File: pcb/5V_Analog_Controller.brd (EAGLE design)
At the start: 50 x 36 mm, 26 parts, among them J1 POWER, Q1 AO3400, Q2 AO3400, U1 ESP32-PICO-MINI-02, U2 AP2112K, X1 PROG, X2 SS-52100-001, X3 SS-52100-001, X5 BOOT, X6 RESET

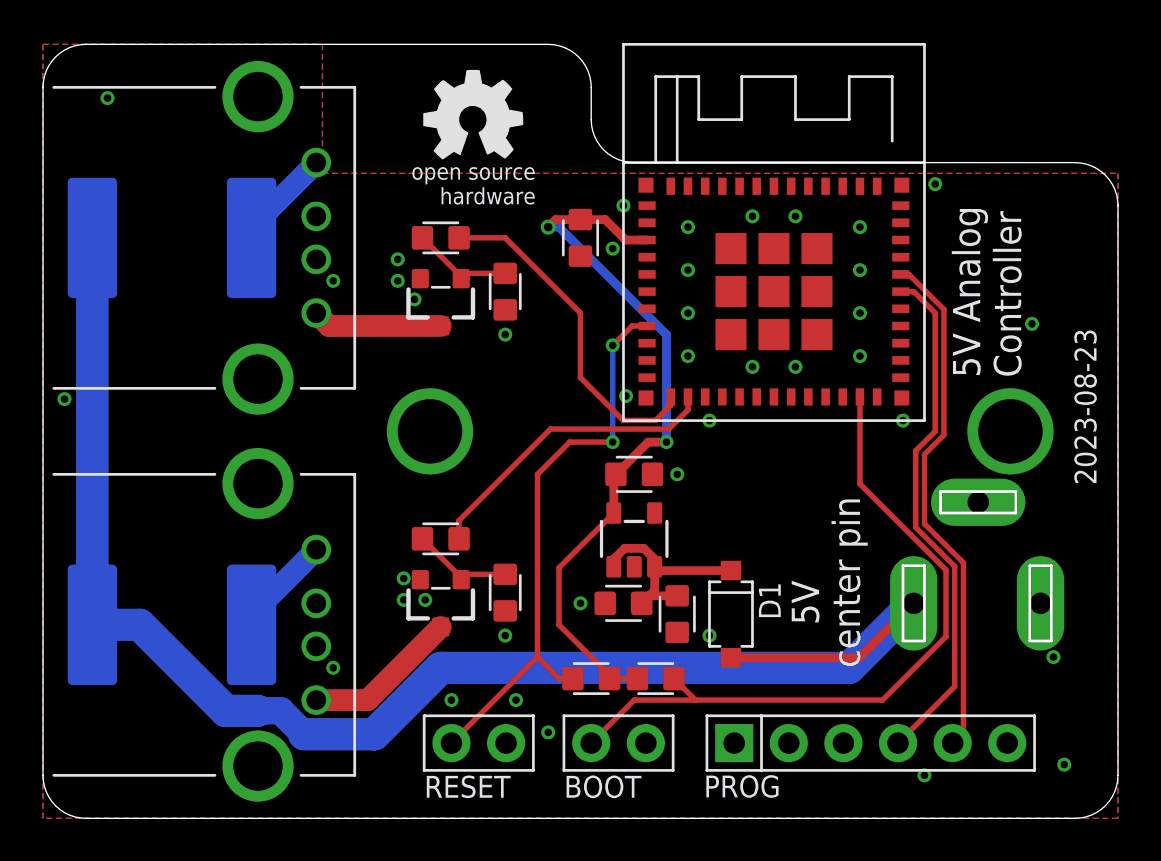
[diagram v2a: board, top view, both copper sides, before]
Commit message: Add second PTC footprint
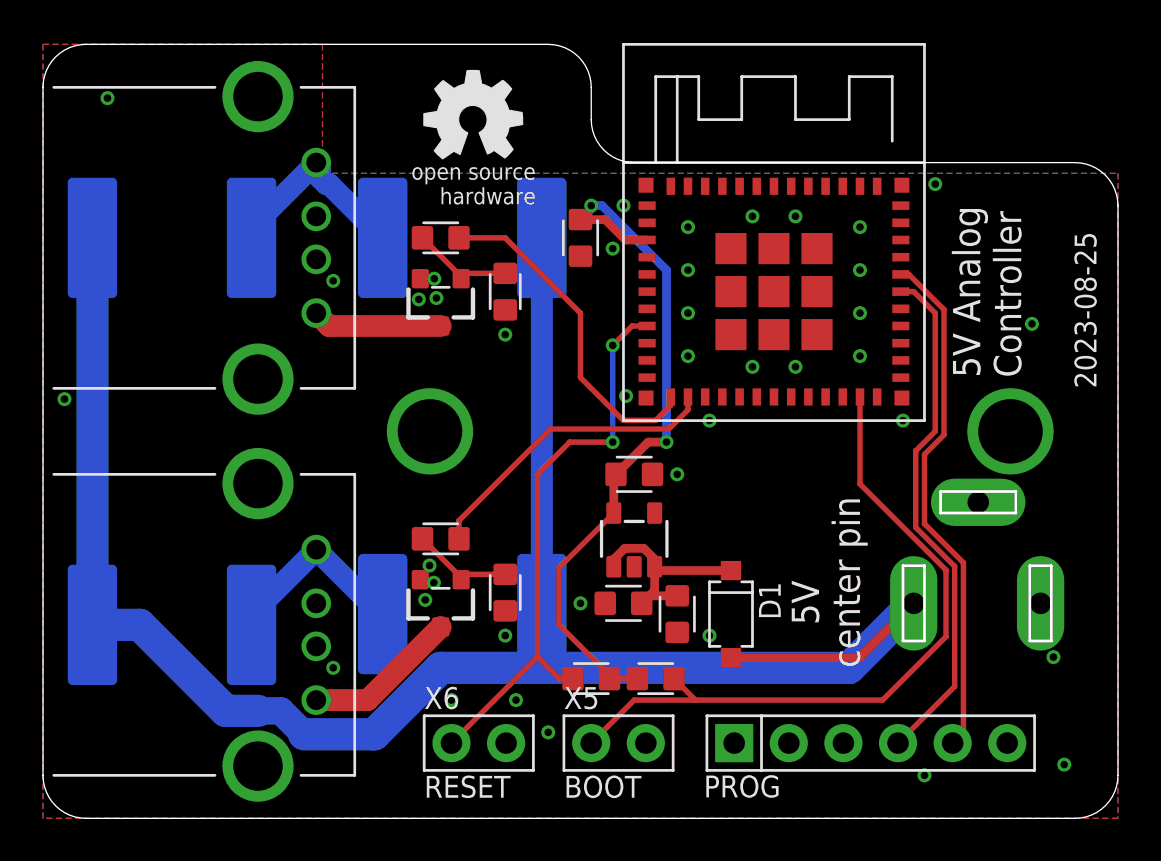
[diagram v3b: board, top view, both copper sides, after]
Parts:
- added F3, F4: JK-SMD300L-16, M2M-Fuse:JK-SMD300
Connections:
- net N$5: now also F3.B
- net N$6: now also F4.B
- net VSW: now also F3.A, F4.A
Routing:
- net VSW: track 70.4 -> 90.7 mm
- net N$5: track 4.75 -> 9.60 mm
- net N$6: track 4.75 -> 9.08 mm
- net VCC: track 33.6 -> 33.0 mm
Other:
- board text added: "2023-08-25"
- board text removed: "2023-08-23"
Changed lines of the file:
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@@
 <text x="45.5" y="20.5" size="1.27" layer="21" rot="R90">5V Analog
 Controller</text>
-<text x="49" y="15.5" size="1.016" layer="21" rot="R90">2023-08-23</text>
+<text x="49" y="20" size="1.016" layer="21" rot="R90">2023-08-25</text>
 <text x="38" y="7" size="1.27" layer="21" rot="R90">    5V
 center pin</text>
@@
 </element>
 <element name="X5" library="M2M-Connectors" package="1X02-2.54" value="BOOT" x="25.5" y="3.5" smashed="yes">
-<attribute name="NAME" x="24.23" y="5.0875" size="1.016" layer="25"/>
 <attribute name="NAME" x="24.611" y="2.865" size="1.27" layer="48"/>
 <attribute name="NAME" x="24.865" y="2.865" size="0.8128" layer="51"/>
+<attribute name="NAME" x="24.23" y="5.0875" size="1.016" layer="25"/>
 <attribute name="VALUE" x="24.23" y="0.96" size="1.016" layer="21"/>
 </element>
 <element name="X6" library="M2M-Connectors" package="1X02-2.54" value="RESET" x="19" y="3.5" smashed="yes">
-<attribute name="NAME" x="17.73" y="5.0875" size="1.016" layer="25"/>
 <attribute name="NAME" x="18.111" y="2.865" size="1.27" layer="48"/>
 <attribute name="NAME" x="18.865" y="2.365" size="0.8128" layer="51"/>
+<attribute name="NAME" x="17.73" y="5.0875" size="1.016" layer="25"/>
 <attribute name="VALUE" x="17.73" y="0.96" size="1.016" layer="21"/>
 </element>
@@
 <attribute name="NAME" x="33.3" y="11" size="1.016" layer="21" rot="R270"/>
 <attribute name="VALUE" x="29.7" y="11" size="1.016" layer="27" rot="R270"/>
+</element>
+<element name="F3" library="M2M-Fuse" package="JK-SMD300" value="JK-SMD300L-16" x="19.5" y="27" smashed="yes" rot="MR0">
+<attribute name="NAME" x="24.5" y="30.5" size="1.016" layer="26" rot="MR0"/>
+<attribute name="NAME" x="19.5" y="27" size="1.016" layer="48" rot="MR0" align="center"/>
+<attribute name="VALUE" x="24.5" y="22.5" size="1.016" layer="28" rot="MR0"/>
+</element>
+<element name="F4" library="M2M-Fuse" package="JK-SMD300" value="JK-SMD300L-16" x="19.5" y="9.5" smashed="yes" rot="MR0">
+<attribute name="NAME" x="24.5" y="13" size="1.016" layer="26" rot="MR0"/>
+<attribute name="NAME" x="19.5" y="9.5" size="1.016" layer="48" rot="MR0" align="center"/>
+<attribute name="VALUE" x="24.5" y="5" size="1.016" layer="28" rot="MR0"/>
 </element>
 </elements>
@@
 <wire x1="26.15" y1="27.85" x2="25" y2="27.85" width="0.4064" layer="1"/>
 <wire x1="27.1" y1="26.9" x2="26.15" y2="27.85" width="0.4064" layer="1"/>
-<wire x1="25" y1="27.85" x2="23.85" y2="27.85" width="0.4064" layer="1"/>
-<wire x1="23.85" y1="27.85" x2="23.5" y2="27.5" width="0.4064" layer="1"/>
-<via x="23.5" y="27.5" extent="1-16" drill="0.4"/>
 <contactref element="U2" pad="5"/>
 <contactref element="C4" pad="1"/>
@@
 <wire x1="28.15" y1="17.5" x2="29" y2="17.5" width="0.4064" layer="1"/>
 <via x="29" y="17.5" extent="1-16" drill="0.35"/>
-<wire x1="29" y1="17.5" x2="29" y2="22.5" width="0.4064" layer="16"/>
-<wire x1="29" y1="22.5" x2="24" y2="27.5" width="0.4064" layer="16"/>
-<wire x1="24" y1="27.5" x2="23.5" y2="27.5" width="0.4064" layer="16"/>
 <contactref element="R5" pad="2"/>
 <contactref element="R6" pad="2"/>
@@
 <wire x1="26.5" y1="6.5" x2="27.65" y2="6.5" width="0.254" layer="1"/>
 <wire x1="26.55" y1="14.2" x2="24" y2="11.65" width="0.254" layer="1"/>
-<wire x1="24" y1="9" x2="25.75" y2="7.25" width="0.254" layer="1"/>
-<wire x1="25.75" y1="7.25" x2="26.5" y2="6.5" width="0.254" layer="1"/>
+<wire x1="24" y1="9" x2="26.5" y2="6.5" width="0.254" layer="1"/>
 <wire x1="24" y1="11.65" x2="24" y2="9" width="0.254" layer="1"/>
+<wire x1="29" y1="25.5" x2="26" y2="28.5" width="0.4064" layer="16"/>
+<wire x1="26" y1="28.5" x2="25.5" y2="28.5" width="0.4064" layer="16"/>
+<via x="25.5" y="28.5" extent="1-16" drill="0.35"/>
+<wire x1="25.5" y1="28.5" x2="25.5" y2="28.35" width="0.4064" layer="1"/>
+<wire x1="25.5" y1="28.35" x2="25" y2="27.85" width="0.4064" layer="1"/>
+<wire x1="29" y1="17.5" x2="29" y2="25.5" width="0.4064" layer="16"/>
 </signal>
 <signal name="GND">
@@
 <via x="1" y="19.5" extent="1-16" drill="0.35"/>
 <via x="3" y="33.5" extent="1-16" drill="0.35"/>
-<via x="16.5" y="25" extent="1-16" drill="0.35"/>
-<via x="16.5" y="26" extent="1-16" drill="0.35"/>
-<via x="17.28" y="24.138" extent="1-16" drill="0.35"/>
+<via x="18.3" y="24.2" extent="1-16" drill="0.35"/>
+<via x="18.2" y="25.1" extent="1-16" drill="0.35"/>
+<via x="17.48" y="24.138" extent="1-16" drill="0.35"/>
 <via x="17.78" y="10.16" extent="1-16" drill="0.35"/>
-<via x="16.78" y="11.16" extent="1-16" drill="0.35"/>
-<via x="16.78" y="10.16" extent="1-16" drill="0.35"/>
+<via x="17.98" y="11.76" extent="1-16" drill="0.35"/>
+<via x="18.18" y="10.96" extent="1-16" drill="0.35"/>
 <contactref element="U2" pad="2"/>
 <contactref element="C4" pad="2"/>
@@
 <wire x1="12.71" y1="30.5" x2="9.7" y2="27.49" width="1.016" layer="16"/>
 <wire x1="9.7" y1="27.49" x2="9.7" y2="27" width="1.016" layer="16"/>
+<contactref element="F3" pad="B"/>
+<wire x1="12.71" y1="30.5" x2="12.892" y2="30.318" width="1.016" layer="16"/>
+<wire x1="12.892" y1="30.318" x2="12.892" y2="29.78958125" width="1.016" layer="16"/>
+<wire x1="12.892" y1="29.78958125" x2="13.18958125" y2="29.492" width="1.016" layer="16"/>
+<wire x1="13.18958125" y1="29.492" x2="13.308" y2="29.492" width="1.016" layer="16"/>
+<wire x1="13.308" y1="29.492" x2="15.8" y2="27" width="1.016" layer="16"/>
 </signal>
 <signal name="N$6">
@@
 <wire x1="12.71" y1="12.5" x2="9.7" y2="9.49" width="1.016" layer="16"/>
 <wire x1="9.7" y1="9.49" x2="9.7" y2="9" width="1.016" layer="16"/>
+<contactref element="F4" pad="B"/>
+<wire x1="12.71" y1="12.5" x2="15.71" y2="9.5" width="1.016" layer="16"/>
+<wire x1="15.71" y1="9.5" x2="15.8" y2="9.5" width="1.016" layer="16"/>
 </signal>
 <signal name="VSW">
@@
 <wire x1="2.3" y1="27" x2="2.3" y2="9" width="1.5" layer="16"/>
 <wire x1="40.5" y1="10" x2="37.5" y2="7" width="1.5" layer="16"/>
-<wire x1="37.5" y1="7" x2="18.5" y2="7" width="1.5" layer="16"/>
+<wire x1="37.5" y1="7" x2="24" y2="7" width="1.5" layer="16"/>
+<wire x1="24" y1="7" x2="18.5" y2="7" width="1.5" layer="16"/>
 <wire x1="18.5" y1="7" x2="15.4076" y2="3.9076" width="1.5" layer="16"/>
 <wire x1="12.14335625" y1="3.9076" x2="15.4076" y2="3.9076" width="1.5" layer="16"/>
@@
 <wire x1="11.05095625" y1="5" x2="12.14335625" y2="3.9076" width="1.27" layer="16"/>
 <wire x1="4.5" y1="9" x2="8.5" y2="5" width="1.5" layer="16"/>
+<contactref element="F3" pad="A"/>
+<contactref element="F4" pad="A"/>
+<wire x1="23.2" y1="27" x2="23.2" y2="9.5" width="1.016" layer="16"/>
+<wire x1="23.2" y1="9.5" x2="23.2" y2="7.8" width="1.016" layer="16"/>
+<wire x1="23.2" y1="7.8" x2="24" y2="7" width="1.016" layer="16"/>
 </signal>
 </signals>

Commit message: Increase current capablity
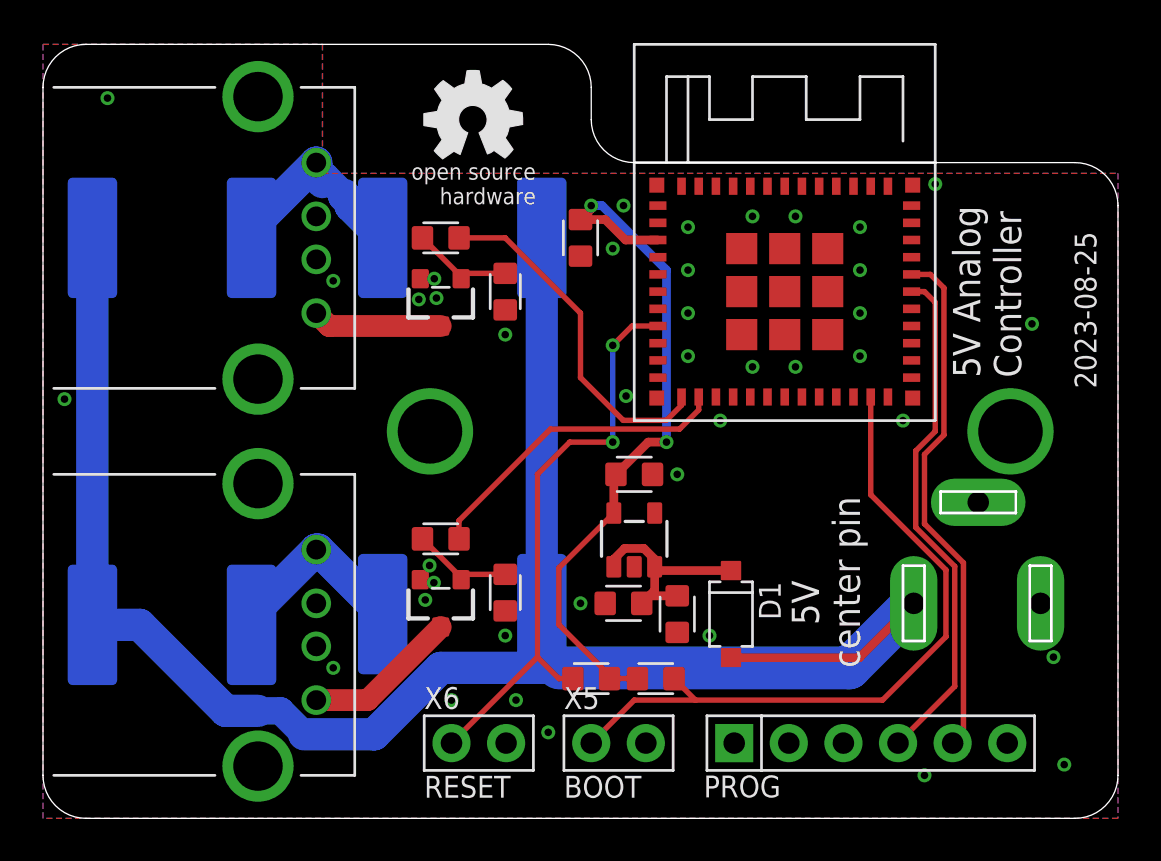
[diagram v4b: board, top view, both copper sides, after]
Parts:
- moved U1 0.50 mm to (34.5, 24.5)
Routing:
- net N$5: track 9.60 -> 10.2 mm
- net VCC: track 33.0 -> 33.5 mm
- net L2: track 14.2 -> 14.7 mm
- net L1: track 15.8 -> 16.3 mm
- net EN: track 26.8 -> 27.3 mm
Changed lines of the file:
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@@
 <drawing>
 <settings>
-<setting alwaysvectorfont="yes"/>
+<setting alwaysvectorfont="no"/>
 <setting verticaltext="up"/>
 </settings>
@@
 <attribute name="VALUE" x="18.5" y="14.905" size="1.016" layer="27" rot="R180" align="bottom-center"/>
 </element>
-<element name="U1" library="M2M-Modules" package="ESP32-PICO-MINI-02" value="ESP32-PICO-MINI-02" x="34" y="24.5" smashed="yes"/>
+<element name="U1" library="M2M-Modules" package="ESP32-PICO-MINI-02" value="ESP32-PICO-MINI-02" x="34.5" y="24.5" smashed="yes"/>
 <element name="X1" library="M2M-Connectors" package="FTDI232-1X06" value="PROG" x="38.5" y="3.5" smashed="yes" rot="R90">
 <attribute name="NAME" x="29.9275" y="2.23" size="1.016" layer="26" rot="R90"/>
@@
 <contactref element="U1" pad="3"/>
 <contactref element="C1" pad="1"/>
-<wire x1="28.1" y1="26.9" x2="27.1" y2="26.9" width="0.4064" layer="1"/>
+<wire x1="28.6" y1="26.9" x2="27.1" y2="26.9" width="0.4064" layer="1"/>
 <wire x1="26.15" y1="27.85" x2="25" y2="27.85" width="0.4064" layer="1"/>
 <wire x1="27.1" y1="26.9" x2="26.15" y2="27.85" width="0.4064" layer="1"/>
@@
 <via x="27" y="28.5" extent="1-16" drill="0.35"/>
 <via x="40" y="18.5" extent="1-16" drill="0.35"/>
-<via x="31" y="18.5" extent="1-16" drill="0.35"/>
+<via x="31.5" y="18.5" extent="1-16" drill="0.35"/>
 <via x="27.119" y="19.643" extent="1-16" drill="0.35"/>
 <via x="47.5" y="2.5" extent="1-16" drill="0.35"/>
@@
 <wire x1="39.05076875" y1="5.5" x2="42" y2="8.44923125" width="0.254" layer="1"/>
 <wire x1="42" y1="8.44923125" x2="42" y2="11.55076875" width="0.254" layer="1"/>
-<wire x1="42" y1="11.55076875" x2="38" y2="15.55076875" width="0.254" layer="1"/>
-<wire x1="38" y1="15.55076875" x2="38" y2="19.6" width="0.254" layer="1"/>
+<wire x1="42" y1="11.55076875" x2="38.5" y2="15.05076875" width="0.254" layer="1"/>
+<wire x1="38.5" y1="15.05076875" x2="38.5" y2="19.6" width="0.254" layer="1"/>
 </signal>
 <signal name="EN">
 <contactref element="U1" pad="8"/>
 <contactref element="X6" pad="1"/>
-<wire x1="28.1" y1="22.9" x2="27.4" y2="22.9" width="0.254" layer="1"/>
+<wire x1="28.6" y1="22.9" x2="27.4" y2="22.9" width="0.254" layer="1"/>
 <wire x1="27.4" y1="22.9" x2="26.5" y2="22" width="0.254" layer="1"/>
 <via x="26.5" y="22" extent="1-16" drill="0.35"/>
@@
 <contactref element="U1" pad="31"/>
 <contactref element="X1" pad="RX"/>
-<wire x1="39.9" y1="25.3" x2="40" y2="25.3" width="0.254" layer="1"/>
+<wire x1="40.4" y1="25.3" x2="40.2747375" y2="25.3" width="0.254" layer="1"/>
 <wire x1="42.31" y1="3.5" x2="42.8128" y2="4.0028" width="0.254" layer="1"/>
 <wire x1="42.8128" y1="4.0028" x2="42.8128" y2="11.88744375" width="0.254" layer="1"/>
 <wire x1="42.8128" y1="11.88744375" x2="41" y2="13.70024375" width="0.254" layer="1"/>
-<wire x1="41.9064" y1="17.8316625" x2="41.9064" y2="23.6683375" width="0.254" layer="1"/>
-<wire x1="40.2747375" y1="25.3" x2="40" y2="25.3" width="0.254" layer="1"/>
+<wire x1="41.9064" y1="17.8316625" x2="41.9064" y2="24.6683375" width="0.254" layer="1"/>
+<wire x1="41.2747375" y1="25.3" x2="40.4" y2="25.3" width="0.254" layer="1"/>
+<wire x1="40.4" y1="25.3" x2="40.5" y2="25.3" width="0.254" layer="1"/>
 <wire x1="41" y1="13.70024375" x2="41" y2="16.9252625" width="0.254" layer="1"/>
 <wire x1="41" y1="16.9252625" x2="41.9064" y2="17.8316625" width="0.254" layer="1"/>
-<wire x1="41.9064" y1="23.6683375" x2="40.2747375" y2="25.3" width="0.254" layer="1"/>
+<wire x1="41.9064" y1="24.6683375" x2="41.2747375" y2="25.3" width="0.254" layer="1"/>
 </signal>
 <signal name="RXD0">
@@
 <wire x1="39.77" y1="3.5" x2="42.4064" y2="6.1364" width="0.254" layer="1"/>
 <wire x1="42.4064" y1="11.71910625" x2="42.4064" y2="6.1364" width="0.254" layer="1"/>
-<wire x1="39.9" y1="24.5" x2="40.5" y2="24.5" width="0.254" layer="1"/>
-<wire x1="41.5" y1="23.5" x2="41.5" y2="18" width="0.254" layer="1"/>
-<wire x1="40.5" y1="24.5" x2="41.5" y2="23.5" width="0.254" layer="1"/>
+<wire x1="40.4" y1="24.5" x2="41" y2="24.5" width="0.254" layer="1"/>
+<wire x1="41.5" y1="24" x2="41.5" y2="18" width="0.254" layer="1"/>
+<wire x1="41" y1="24.5" x2="41.5" y2="24" width="0.254" layer="1"/>
 <wire x1="41.5" y1="18" x2="40.5936" y2="17.0936" width="0.254" layer="1"/>
 <wire x1="40.5936" y1="17.0936" x2="40.5936" y2="13.53190625" width="0.254" layer="1"/>
@@
 <wire x1="21.5" y1="27" x2="19.35" y2="27" width="0.254" layer="1"/>
 <contactref element="U1" pad="12"/>
-<wire x1="29.2" y1="19.6" x2="29.2" y2="19.2132" width="0.254" layer="1"/>
-<wire x1="29.2" y1="19.2132" x2="28.5" y2="18.5132" width="0.254" layer="1"/>
-<wire x1="28.5" y1="18.5132" x2="26.9868" y2="18.5132" width="0.254" layer="1"/>
+<wire x1="29.7" y1="19.6" x2="29.7" y2="19.2132" width="0.254" layer="1"/>
+<wire x1="29.7" y1="19.2132" x2="29" y2="18.5132" width="0.254" layer="1"/>
+<wire x1="29" y1="18.5132" x2="26.9868" y2="18.5132" width="0.254" layer="1"/>
 <wire x1="26.9868" y1="18.5132" x2="25" y2="20.5" width="0.254" layer="1"/>
 <wire x1="25" y1="20.5" x2="25" y2="23.5" width="0.254" layer="1"/>
@@
 <wire x1="19.35" y1="13" x2="19.35" y2="13.85" width="0.254" layer="1"/>
 <contactref element="U1" pad="13"/>
-<wire x1="30" y1="19" x2="30" y2="19.6" width="0.254" layer="1"/>
+<wire x1="30.5" y1="19" x2="30.5" y2="19.6" width="0.254" layer="1"/>
 <wire x1="19.35" y1="13.85" x2="23.6068" y2="18.1068" width="0.254" layer="1"/>
-<wire x1="23.6068" y1="18.1068" x2="29.1068" y2="18.1068" width="0.254" layer="1"/>
-<wire x1="29.1068" y1="18.1068" x2="30" y2="19" width="0.254" layer="1"/>
+<wire x1="23.6068" y1="18.1068" x2="29.6068" y2="18.1068" width="0.254" layer="1"/>
+<wire x1="29.6068" y1="18.1068" x2="30.5" y2="19" width="0.254" layer="1"/>
 </signal>
 <signal name="NC">
@@
 <contactref element="X2" pad="1"/>
 <contactref element="F1" pad="B"/>
-<wire x1="12.71" y1="30.5" x2="9.7" y2="27.49" width="1.016" layer="16"/>
-<wire x1="9.7" y1="27.49" x2="9.7" y2="27" width="1.016" layer="16"/>
 <contactref element="F3" pad="B"/>
-<wire x1="12.71" y1="30.5" x2="12.892" y2="30.318" width="1.016" layer="16"/>
-<wire x1="12.892" y1="30.318" x2="12.892" y2="29.78958125" width="1.016" layer="16"/>
-<wire x1="12.892" y1="29.78958125" x2="13.18958125" y2="29.492" width="1.016" layer="16"/>
-<wire x1="13.18958125" y1="29.492" x2="13.308" y2="29.492" width="1.016" layer="16"/>
-<wire x1="13.308" y1="29.492" x2="15.8" y2="27" width="1.016" layer="16"/>
+<wire x1="12.71" y1="30.5" x2="9.7" y2="27.49" width="1.5" layer="16"/>
+<wire x1="9.7" y1="27.49" x2="9.7" y2="27" width="1.5" layer="16"/>
+<wire x1="12.71" y1="30.5" x2="12.71" y2="29.8824" width="1.5" layer="16"/>
+<wire x1="12.71" y1="29.8824" x2="13" y2="29.5924" width="1.5" layer="16"/>
+<wire x1="15.8" y1="27" x2="14.3024" y2="28.4976" width="1.5" layer="16"/>
+<wire x1="14.3024" y1="28.4976" x2="14.3024" y2="28.65959375" width="1.5" layer="16"/>
+<wire x1="14.3024" y1="28.65959375" x2="14" y2="28.96199375" width="1.5" layer="16"/>
+<wire x1="14" y1="28.96199375" x2="14" y2="29" width="1.5" layer="16"/>
+<wire x1="14" y1="29" x2="13.1176" y2="29.8824" width="1.27" layer="16"/>
+<wire x1="13.1176" y1="29.8824" x2="12.71" y2="29.8824" width="1.27" layer="16"/>
 </signal>
 <signal name="N$6">
 <contactref element="X3" pad="1"/>
 <contactref element="F2" pad="B"/>
-<wire x1="12.71" y1="12.5" x2="9.7" y2="9.49" width="1.016" layer="16"/>
-<wire x1="9.7" y1="9.49" x2="9.7" y2="9" width="1.016" layer="16"/>
 <contactref element="F4" pad="B"/>
-<wire x1="12.71" y1="12.5" x2="15.71" y2="9.5" width="1.016" layer="16"/>
-<wire x1="15.71" y1="9.5" x2="15.8" y2="9.5" width="1.016" layer="16"/>
+<wire x1="9.7" y1="9" x2="9.7" y2="9.49" width="1.5" layer="16"/>
+<wire x1="9.7" y1="9.49" x2="12.71" y2="12.5" width="1.5" layer="16"/>
+<wire x1="15.8" y1="9.5" x2="12.8" y2="12.5" width="1.5" layer="16"/>
+<wire x1="12.8" y1="12.5" x2="12.71" y2="12.5" width="1.5" layer="16"/>
 </signal>
 <signal name="VSW">
@@
 <wire x1="37.975" y1="7.475" x2="40.5" y2="10" width="0.4064" layer="1"/>
 <wire x1="2.3" y1="27" x2="2.3" y2="9" width="1.5" layer="16"/>
-<wire x1="40.5" y1="10" x2="37.5" y2="7" width="1.5" layer="16"/>
-<wire x1="37.5" y1="7" x2="24" y2="7" width="1.5" layer="16"/>
+<wire x1="40.5" y1="10" x2="37.5" y2="7" width="2" layer="16"/>
+<wire x1="37.5" y1="7" x2="24" y2="7" width="2" layer="16"/>
 <wire x1="24" y1="7" x2="18.5" y2="7" width="1.5" layer="16"/>
 <wire x1="18.5" y1="7" x2="15.4076" y2="3.9076" width="1.5" layer="16"/>
@@
 <contactref element="F3" pad="A"/>
 <contactref element="F4" pad="A"/>
-<wire x1="23.2" y1="27" x2="23.2" y2="9.5" width="1.016" layer="16"/>
+<wire x1="23.2" y1="27" x2="23.2" y2="9.5" width="1.5" layer="16"/>
 <wire x1="23.2" y1="9.5" x2="23.2" y2="7.8" width="1.016" layer="16"/>
 <wire x1="23.2" y1="7.8" x2="24" y2="7" width="1.016" layer="16"/>
